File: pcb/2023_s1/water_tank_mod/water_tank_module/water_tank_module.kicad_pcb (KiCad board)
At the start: 2 copper layers, 8 parts, among them J2 Conn_01x05_Male, U4 NRF24L01_Breakout

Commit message: update, added 3d shapes for the pieces, and added capacitor
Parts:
- added C1: C_Polarized, Capacitor_THT:CP_Radial_D5.0mm_P2.50mm, F.Cu at (128.7, 39.9)
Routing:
- net GND5V: track 138.6 -> 140.9 mm

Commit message: added, added fabrication outputs
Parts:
- 5V1, C1, J2, J_DS18, J_EC1, J_esp0, J_esp1, R11, U4: moved to B.Cu
- moved 5V1 82.5 mm to (47.6, 31.0), turned to 0 degrees
- moved C1 79.8 mm to (48.9, 39.9), turned to 0 degrees
- moved R11 71.8 mm to (52.9, 72.8)
- moved J_DS18 63.4 mm to (57.1, 70.2)
- moved J_EC1 63.4 mm to (57.1, 58.0)
- moved J_esp0 57.7 mm to (60.0, 45.6)
- moved U4 35.1 mm to (106.4, 52.9), turned to 0 degrees
- moved J_esp1 25.1 mm to (101.4, 44.7)
- moved J2 4.60 mm to (86.5, 77.6), turned to 180 degrees

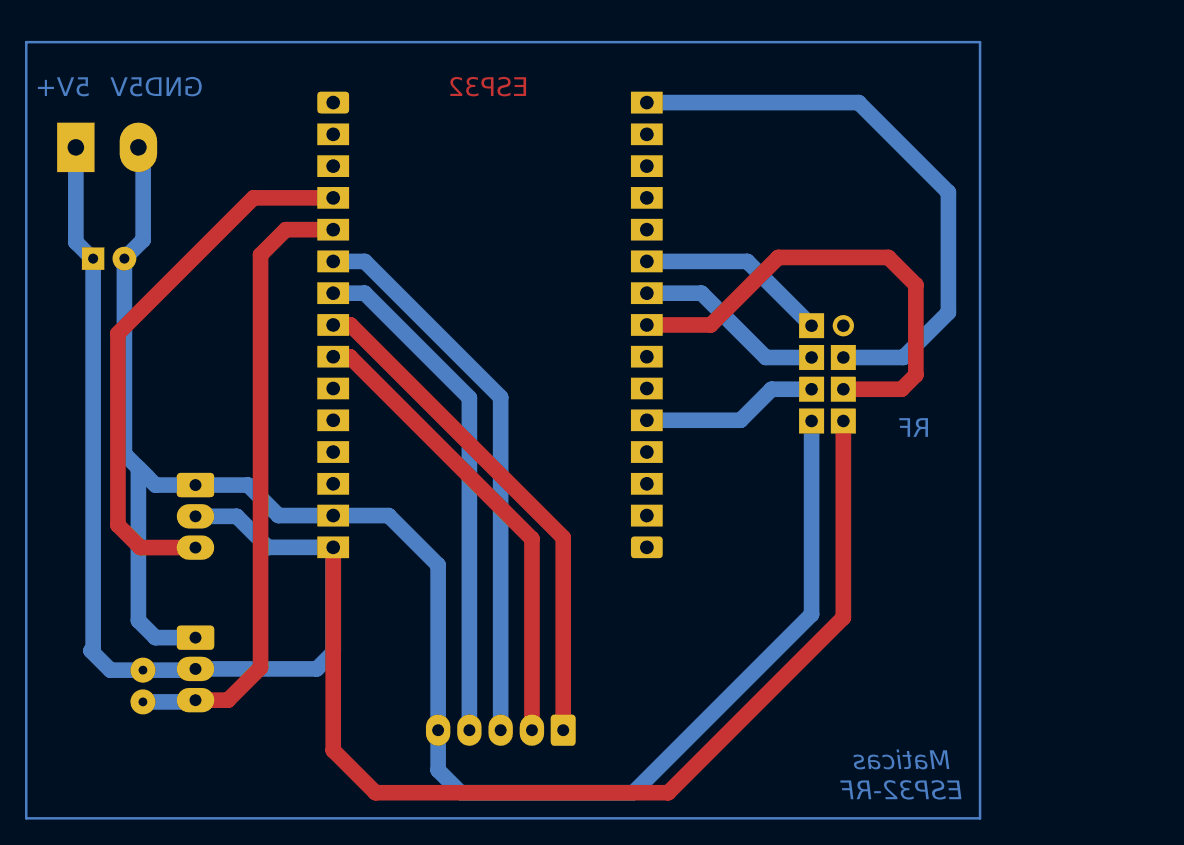
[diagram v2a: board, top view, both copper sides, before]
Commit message: update, added mounting holes
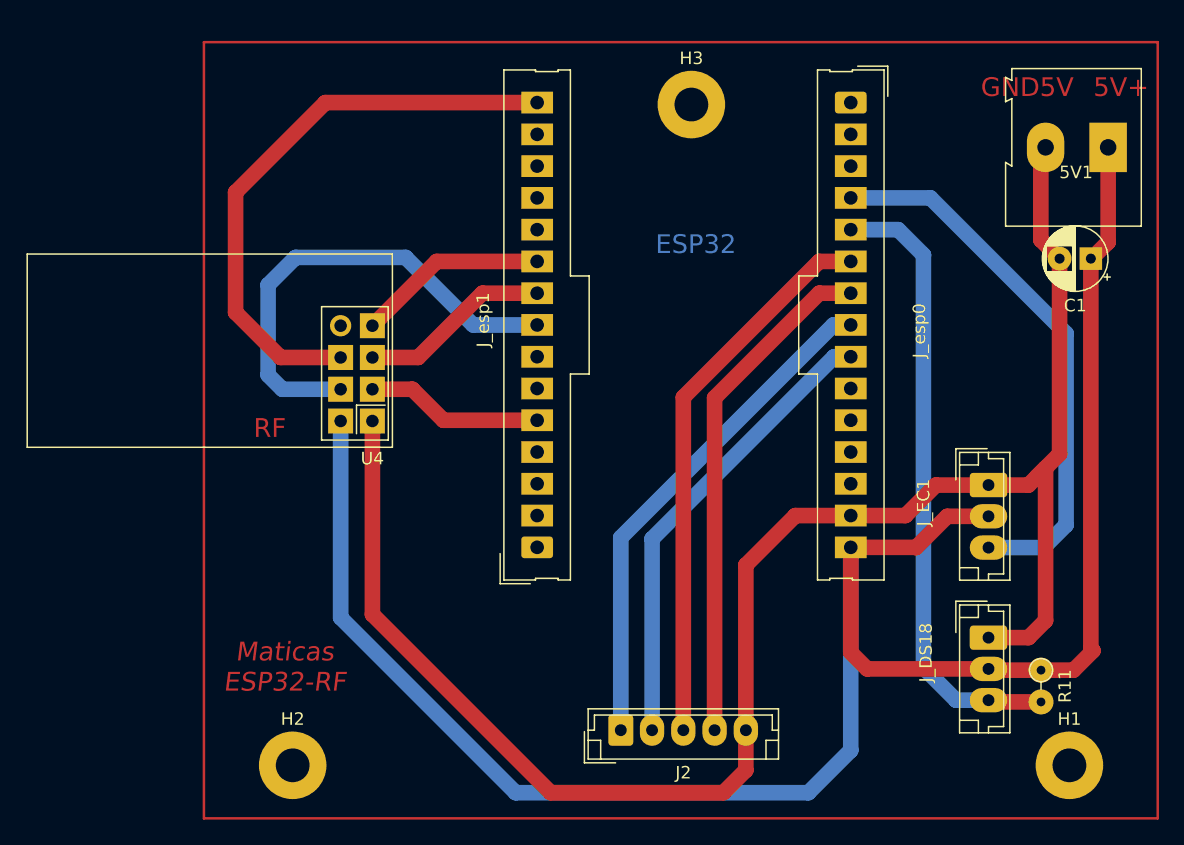
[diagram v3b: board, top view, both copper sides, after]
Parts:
- added H1: MountingHole, MountingHole:MountingHole_2.7mm_M2.5_Pad, F.Cu at (127.0, 80.4)
- added H2: MountingHole, MountingHole:MountingHole_2.7mm_M2.5_Pad, F.Cu at (64.9, 80.4)
- added H3: MountingHole, MountingHole:MountingHole_2.7mm_M2.5_Pad, F.Cu at (96.8, 27.6)
- 5V1, C1, J2, J_DS18, J_EC1, J_esp0, J_esp1, R11, U4: moved to F.Cu
- moved 5V1 82.5 mm to (130.1, 31.0), turned to 180 degrees
- moved C1 79.8 mm to (128.7, 39.9), turned to 180 degrees
- moved R11 71.8 mm to (124.7, 72.8)
- moved J_DS18 63.4 mm to (120.5, 70.2)
- moved J_EC1 63.4 mm to (120.5, 58.0)
- moved J_esp0 57.7 mm to (117.7, 45.6)
- moved U4 35.1 mm to (71.3, 52.9), turned to 180 degrees
- moved J_esp1 25.1 mm to (76.3, 44.7)
- moved J2 4.60 mm to (91.1, 77.6), turned to 0 degrees

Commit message: update, finished connecting the power pcb module, and added the fan control to both pcbs
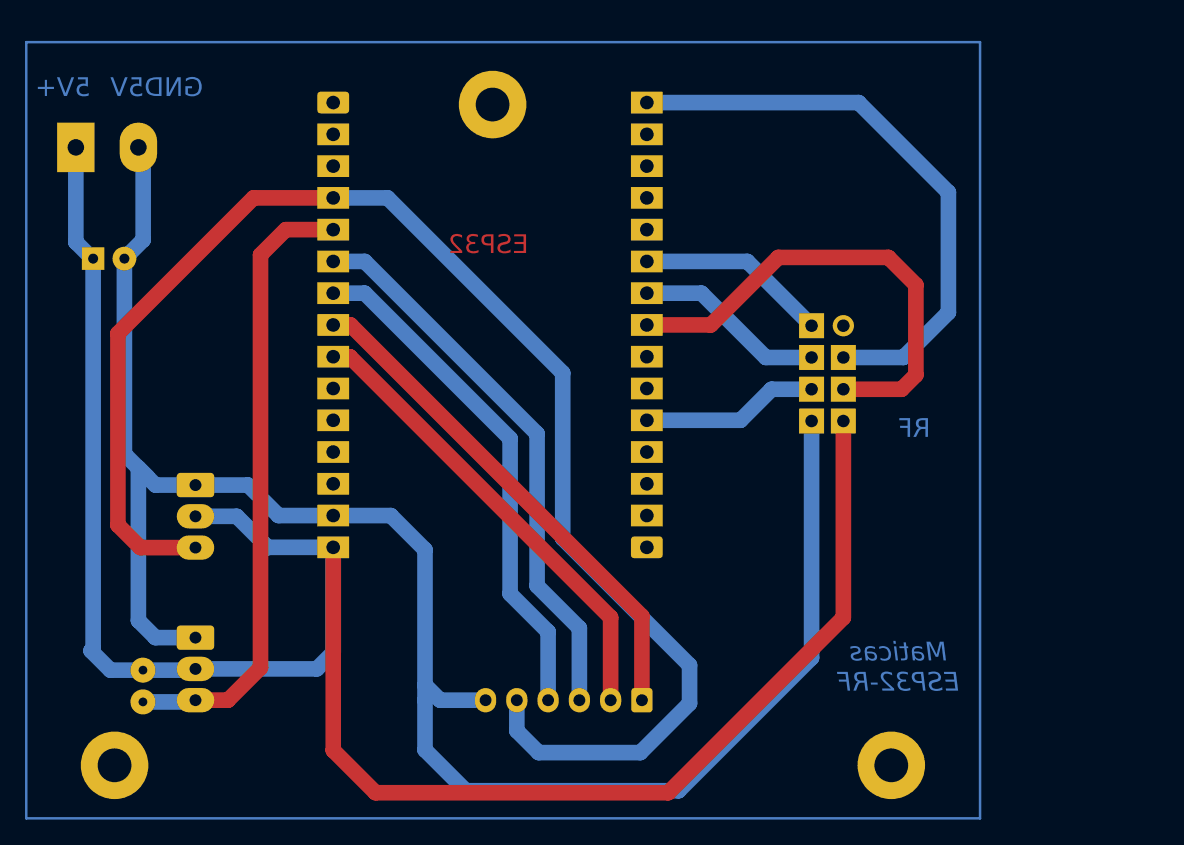
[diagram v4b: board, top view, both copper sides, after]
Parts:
- removed J2: Conn_01x05_Male, Connector_JST:JST_EH_B5B-EH-A_1x05_P2.50mm_Vertical
- added J1: Conn_01x06_Male, Connector_JST:JST_EH_B6B-EH-A_1x06_P2.50mm_Vertical, B.Cu at (92.8, 75.2)
- 5V1, C1, H1, H2, H3, J_DS18, J_EC1, J_esp0, J_esp1, R11, U4: moved to B.Cu
- moved 5V1 82.5 mm to (47.6, 31.0), turned to 0 degrees
- moved C1 79.8 mm to (48.9, 39.9), turned to 0 degrees
- moved H1 76.3 mm to (50.7, 80.4), turned to 180 degrees
- moved R11 71.8 mm to (52.9, 72.8)
- moved J_DS18 63.4 mm to (57.1, 70.2)
- moved J_EC1 63.4 mm to (57.1, 58.0)
- moved J_esp0 57.7 mm to (60.0, 45.6)
- moved H2 47.9 mm to (112.8, 80.4), turned to 180 degrees
- moved U4 35.1 mm to (106.4, 52.9), turned to 0 degrees
- moved J_esp1 25.1 mm to (101.4, 44.7)
- moved H3 15.9 mm to (80.9, 27.6), turned to 180 degrees
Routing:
- net D34: track 44.0 -> 117.3 mm
- net GND5V: track 140.9 -> 147.9 mm

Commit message: fix, fixed positioning of esp32, it was mirrored
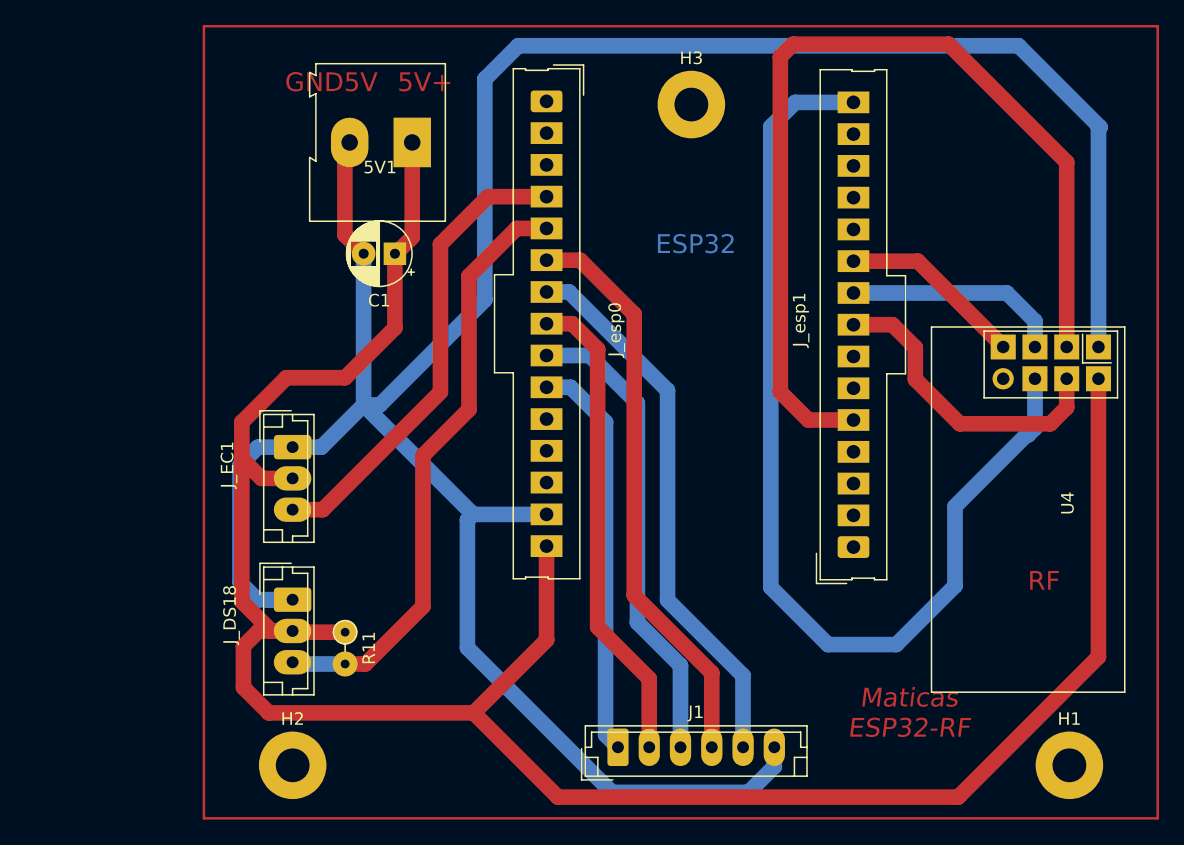
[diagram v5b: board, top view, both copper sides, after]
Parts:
- 5V1, C1, H1, H2, H3, J1, J_DS18, J_EC1, J_esp0, J_esp1, R11, U4: moved to F.Cu
- moved H1 76.3 mm to (127.0, 80.4), turned to 0 degrees
- moved H2 47.9 mm to (64.9, 80.4), turned to 0 degrees
- moved J_esp0 33.4 mm to (93.3, 45.5)
- moved 5V1 26.9 mm to (74.5, 30.6), turned to 180 degrees
- moved C1 24.1 mm to (73.1, 39.5), turned to 180 degrees
- moved U4 23.7 mm to (129.3, 46.9), turned to -90 degrees
- moved R11 16.4 mm to (69.1, 69.7)
- moved H3 15.9 mm to (96.8, 27.6), turned to 0 degrees
- moved J_DS18 8.33 mm to (64.9, 67.1)
- moved J_EC1 8.33 mm to (64.9, 54.9)
- moved J1 4.22 mm to (90.9, 78.9), turned to 0 degrees
- moved J_esp1 0.22 mm to (101.6, 44.7)
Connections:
- J1 pad 1: D25 -> D27
- J1 pad 2: D26 -> D25
- J1 pad 3: D32 -> D26
- J1 pad 4: D33 -> D32
- J1 pad 5: D34 -> D33
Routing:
- net D34: track 117.3 -> 37.6 mm
- net GND5V: track 147.9 -> 212.1 mm
- net D4: track 14.2 -> 75.6 mm
- net D23: track 46.6 -> 82.1 mm
- net D27: track 0.00 -> 32.3 mm
- net 5v: track 162.0 -> 181.5 mm
- net D5: track 38.1 -> 24.7 mm
- net D33: track 41.1 -> 44.0 mm
- net D25: track 41.2 -> 38.5 mm
- net D18: track 15.3 -> 17.5 mm
- net D35: track 50.2 -> 48.3 mm
- net D32: track 44.7 -> 46.0 mm

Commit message: fix, separated the light control into another pcb, due to the different voltage it handles and confort for the use
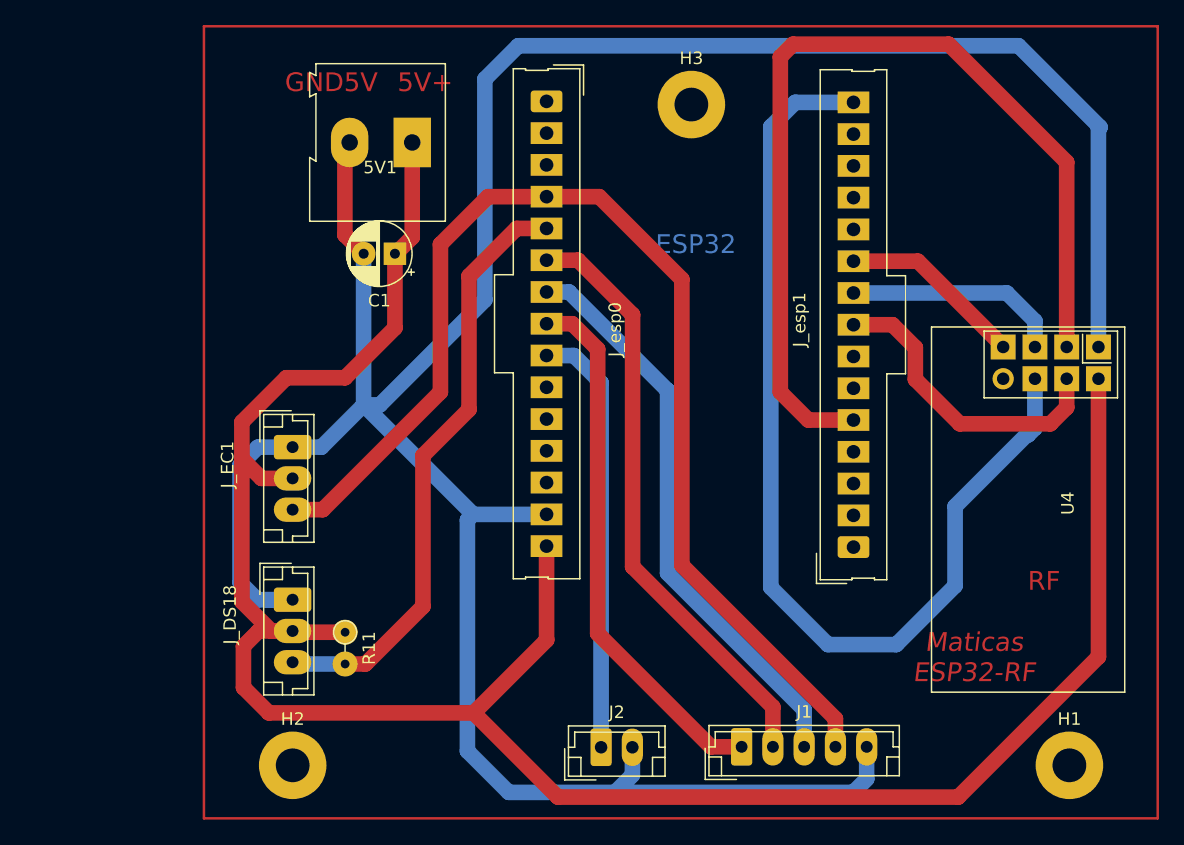
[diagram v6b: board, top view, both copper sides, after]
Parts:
- added J2: Conn_01x02_Male, Connector_JST:JST_EH_B2B-EH-A_1x02_P2.50mm_Vertical, F.Cu at (89.6, 78.9)
- J1: value Conn_01x06_Male -> Conn_01x05_Male; footprint Connector_JST:JST_EH_B6B-EH-A_1x06_P2.50mm_Vertical -> Connector_JST:JST_EH_B5B-EH-A_1x05_P2.50mm_Vertical
- moved J1 9.89 mm to (100.8, 78.9)
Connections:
- J1 pad 1: D27 -> D25
- J1 pad 2: D25 -> D32
- J1 pad 3: D26 -> D33
- J1 pad 4: D32 -> D34
- J1 pad 5: D33 -> GND5V
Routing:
- net D34: track 37.6 -> 93.6 mm
- net D27: track 32.3 -> 0.00 mm
- net GND5V: track 212.1 -> 229.1 mm
- net D25: track 38.5 -> 42.9 mm
- net D26: track 37.8 -> 34.4 mm
- net D33: track 44.0 -> 46.0 mm
- net D32: track 46.0 -> 47.9 mm
